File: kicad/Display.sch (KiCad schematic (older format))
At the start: 5 parts, among them SW301 SW_PUSH, U301 EA_DOGMxxx-A

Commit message: Change over to use the DOGM081 adapter board rather than direct connect - also used the CE_Socket!
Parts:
- removed C301: 0.1~~1μF, Capacitors_SMD:C_1206, symbol C
- removed C302: 0.47~~2.2μF, Capacitors_SMD:C_1206, symbol C
- removed U301: EA_DOGMxxx-A, FieldDevice_Footprints:EA_DOGM081x-A, symbol EA_DOGMxxx-A
- added P301: CONN_01X06, Pin_Headers:Pin_Header_Straight_1x06_Pitch2.54mm, symbol CONN_01X06
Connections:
- wire segments 37 -> 13
- no-connect marks 4 -> 0
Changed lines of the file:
@@
 Comment4 ""
 $EndDescr
-$Comp
-L EA_DOGMxxx-A U301
-U 1 1 593F5011
-P 5550 2850
-F 0 "U301" H 5400 3450 60  0000 C CNN
-F 1 "EA_DOGMxxx-A" H 5600 2850 60  0000 C CNN
-F 2 "FieldDevice_Footprints:EA_DOGM081x-A" V 4450 5200 60  0001 C CNN
-F 3 "" V 4450 5200 60  0000 C CNN
-F 4 "EA DOGM801W-A" H 5550 2850 60  0001 C CNN "MPN"
-F 5 "Value" H 5550 2850 60  0001 C CNN "Link"
-	1    5550 2850
-	1    0    0    -1
-$EndComp
-NoConn ~ 6350 1800
-NoConn ~ 6250 1800
-NoConn ~ 5150 1800
-NoConn ~ 5050 1800
-Wire Wire Line
-	6650 2700 7200 2700
-Text HLabel 7200 2700 2    60   Input ~ 0
+Text HLabel 5450 2650 0    60   Input ~ 0
+RS
+Text HLabel 5450 2350 0    60   Input ~ 0
 3V3
-Wire Wire Line
-	4450 2150 3850 2150
-$Comp
-L GND #PWR010
-U 1 1 593F50AA
-P 6900 2450
-F 0 "#PWR010" H 6900 2200 50  0001 C CNN
-F 1 "GND" H 6900 2300 50  0000 C CNN
-F 2 "" H 6900 2450 60  0000 C CNN
-F 3 "" H 6900 2450 60  0000 C CNN
-	1    6900 2450
-	1    0    0    -1
-$EndComp
-Wire Wire Line
-	6650 2400 6900 2400
-Wire Wire Line
-	6900 2400 6900 2450
-Wire Wire Line
-	5950 4100 5950 3900
-Wire Wire Line
-	5250 4100 5950 4100
-Wire Wire Line
-	5250 4100 5250 3900
-Wire Wire Line
-	5350 3900 5350 4100
-Connection ~ 5350 4100
-Wire Wire Line
-	5450 3900 5450 4100
-Connection ~ 5450 4100
-Wire Wire Line
-	5550 3900 5550 4100
-Connection ~ 5550 4100
-Wire Wire Line
-	5650 3900 5650 4100
-Connection ~ 5650 4100
-Wire Wire Line
-	5750 3900 5750 4100
-Connection ~ 5750 4100
-$Comp
-L GND #PWR011
-U 1 1 593F5140
-P 6050 4150
-F 0 "#PWR011" H 6050 3900 50  0001 C CNN
-F 1 "GND" H 6050 4000 50  0000 C CNN
-F 2 "" H 6050 4150 60  0000 C CNN
-F 3 "" H 6050 4150 60  0000 C CNN
-	1    6050 4150
-	1    0    0    -1
-$EndComp
-Wire Wire Line
-	6050 3900 6050 4150
-Wire Wire Line
-	6150 3900 6150 4500
-Wire Wire Line
-	6150 4500 5800 4500
-Text HLabel 5800 4500 0    60   Input ~ 0
-RS
-Text HLabel 5500 4300 0    60   Input ~ 0
-3V3
-$Comp
-L GND #PWR012
-U 1 1 593F51AC
-P 3250 2400
-F 0 "#PWR012" H 3250 2150 50  0001 C CNN
-F 1 "GND" H 3250 2250 50  0000 C CNN
-F 2 "" H 3250 2400 60  0000 C CNN
-F 3 "" H 3250 2400 60  0000 C CNN
-	1    3250 2400
-	1    0    0    -1
-$EndComp
-Wire Wire Line
-	3250 2400 3250 2350
-Wire Wire Line
-	3250 2350 4450 2350
-$Comp
-L C C301
-U 1 1 593F51D8
-P 4200 2750
-F 0 "C301" H 4225 2850 50  0000 L CNN
-F 1 "0.1~~1μF" H 4225 2650 50  0000 L CNN
-F 2 "Capacitors_SMD:C_1206" H 4238 2600 30  0001 C CNN
-F 3 "" H 4200 2750 60  0000 C CNN
-F 4 "X7R-G1206 1,0/50" H 4200 2750 60  0001 C CNN "MPN"
-F 5 "Value" H 4200 2750 60  0001 C CNN "Link"
-	1    4200 2750
-	-1   0    0    1
-$EndComp
-Wire Wire Line
-	4450 2600 4200 2600
-Wire Wire Line
-	4200 2900 4450 2900
-$Comp
-L C C302
-U 1 1 593F5875
-P 4200 3350
-F 0 "C302" H 4225 3450 50  0000 L CNN
-F 1 "0.47~~2.2μF" H 4225 3250 50  0000 L CNN
-F 2 "Capacitors_SMD:C_1206" H 4238 3200 30  0001 C CNN
-F 3 "" H 4200 3350 60  0000 C CNN
-F 4 "X7R-G1206 1,0/50" H 4200 3350 60  0001 C CNN "MPN"
-F 5 "Value" H 4200 3350 60  0001 C CNN "Link"
-	1    4200 3350
-	-1   0    0    1
-$EndComp
-Wire Wire Line
-	4200 3200 4450 3200
-Wire Wire Line
-	4200 3500 4450 3500
-Text HLabel 3900 3150 0    60   Input ~ 0
-3V3
-Wire Wire Line
-	3900 3150 4350 3150
-Wire Wire Line
-	4350 3150 4350 3200
-Connection ~ 4350 3200
-Wire Wire Line
-	5500 4300 5600 4300
-Wire Wire Line
-	5600 4300 5600 4100
-Connection ~ 5600 4100
-Wire Wire Line
-	5050 3900 5050 4100
-Wire Wire Line
-	5050 4100 4500 4100
-Wire Wire Line
-	5150 3900 5150 4200
-Wire Wire Line
-	5150 4200 4500 4200
-Text HLabel 4500 4100 0    60   Input ~ 0
+Text HLabel 5450 2450 0    60   Input ~ 0
 MOSI
-Text HLabel 4500 4200 0    60   Input ~ 0
+Text HLabel 5450 2550 0    60   Input ~ 0
 SCK
-Text HLabel 3850 2150 0    60   Input ~ 0
-3V3
-Wire Wire Line
-	6350 3900 6350 4650
-Wire Wire Line
-	6350 4650 5800 4650
-Text HLabel 5800 4650 0    60   Input ~ 0
+Text HLabel 5450 2750 0    60   Input ~ 0
 CS
 $Comp
@@
 $EndComp
 $Comp
-L GND #PWR013
+L GND #PWR010
 U 1 1 593FDBE4
 P 9450 2400
-F 0 "#PWR013" H 9450 2150 50  0001 C CNN
+F 0 "#PWR010" H 9450 2150 50  0001 C CNN
 F 1 "GND" H 9450 2250 50  0000 C CNN
 F 2 "" H 9450 2400 50  0000 C CNN
@@
 	1    0    0    -1
 $EndComp
-Wire Wire Line
-	9250 1500 9450 1500
-Wire Wire Line
-	9450 1500 9450 2400
-Wire Wire Line
-	8650 1500 8150 1500
 Text HLabel 8150 1500 0    60   Input ~ 0
 Display
@@
 $EndComp
 Wire Wire Line
+	9250 1500 9450 1500
+Wire Wire Line
+	9450 1500 9450 2400
+Wire Wire Line
+	8650 1500 8150 1500
+Wire Wire Line
 	8550 2200 8550 2300
 Wire Wire Line
@@
 	8550 1900 8550 1500
 Connection ~ 8550 1500
+$Comp
+L CONN_01X06 P301
+U 1 1 598B33D0
+P 5900 2600
+F 0 "P301" H 5900 2950 50  0000 C CNN
+F 1 "CONN_01X06" V 6000 2600 50  0000 C CNN
+F 2 "Pin_Headers:Pin_Header_Straight_1x06_Pitch2.54mm" H 5900 2600 60  0001 C CNN
+F 3 "" H 5900 2600 60  0000 C CNN
+	1    5900 2600
+	1    0    0    -1
+$EndComp
+Wire Wire Line
+	5700 2350 5450 2350
+Wire Wire Line
+	5700 2450 5450 2450
+Wire Wire Line
+	5700 2550 5450 2550
+Wire Wire Line
+	5700 2650 5450 2650
+Wire Wire Line
+	5700 2750 5450 2750
+Wire Wire Line
+	5700 2850 5400 2850
+Wire Wire Line
+	5400 2850 5400 3000
+$Comp
+L GND #PWR011
+U 1 1 598B3757
+P 5400 3000
+F 0 "#PWR011" H 5400 2750 50  0001 C CNN
+F 1 "GND" H 5400 2850 50  0000 C CNN
+F 2 "" H 5400 3000 60  0000 C CNN
+F 3 "" H 5400 3000 60  0000 C CNN
+	1    5400 3000
+	1    0    0    -1
+$EndComp
 $EndSCHEMATC

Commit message: Enhanced display port connector and layout - Submit to OSH Park
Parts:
- C303: footprint Capacitors_SMD:C_0805 -> Capacitors_SMD:C_0805_HandSoldering
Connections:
- net labels added: SPI_SCK
- net labels removed: SCK
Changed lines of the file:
@@
 MOSI
 Text HLabel 5450 2550 0    60   Input ~ 0
-SCK
+SPI_SCK
 Text HLabel 5450 2750 0    60   Input ~ 0
 CS
@@
 F 0 "C303" H 8575 2150 50  0000 L CNN
 F 1 "0.1μF" H 8575 1950 50  0000 L CNN
-F 2 "Capacitors_SMD:C_0805" H 8588 1900 30  0001 C CNN
+F 2 "Capacitors_SMD:C_0805_HandSoldering" H 8588 1900 30  0001 C CNN
 F 3 "" H 8550 2050 60  0000 C CNN
 	1    8550 2050

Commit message: Altered the display connector for the DOG104 i.e. general purpose
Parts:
- removed P301: CONN_01X06, Pin_Headers:Pin_Header_Straight_1x06_Pitch2.54mm, symbol CONN_01X06
- added P301: Conn_01x07_Female, Pin_Headers:Pin_Header_Angled_1x07_Pitch2.54mm, symbol Conn_01x07_Female
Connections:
- net labels added: MISO
- wire segments 13 -> 14
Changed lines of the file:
@@
 EESchema Schematic File Version 2
+LIBS:FieldDevice-rescue
 LIBS:fieldDevice_symbols
 LIBS:ce_header
@@
 Comment4 ""
 $EndDescr
-Text HLabel 5450 2650 0    60   Input ~ 0
+Text HLabel 5450 2750 0    60   Input ~ 0
 RS
 Text HLabel 5450 2350 0    60   Input ~ 0
@@
 Text HLabel 5450 2450 0    60   Input ~ 0
 MOSI
-Text HLabel 5450 2550 0    60   Input ~ 0
+Text HLabel 5450 2650 0    60   Input ~ 0
 SPI_SCK
-Text HLabel 5450 2750 0    60   Input ~ 0
+Text HLabel 5450 2850 0    60   Input ~ 0
 CS
 $Comp
@@
 $EndComp
 $Comp
-L GND #PWR010
+L GND #PWR09
 U 1 1 593FDBE4
 P 9450 2400
-F 0 "#PWR010" H 9450 2150 50  0001 C CNN
+F 0 "#PWR09" H 9450 2150 50  0001 C CNN
 F 1 "GND" H 9450 2250 50  0000 C CNN
 F 2 "" H 9450 2400 50  0000 C CNN
@@
 	8550 1900 8550 1500
 Connection ~ 8550 1500
-$Comp
-L CONN_01X06 P301
-U 1 1 598B33D0
-P 5900 2600
-F 0 "P301" H 5900 2950 50  0000 C CNN
-F 1 "CONN_01X06" V 6000 2600 50  0000 C CNN
-F 2 "Pin_Headers:Pin_Header_Straight_1x06_Pitch2.54mm" H 5900 2600 60  0001 C CNN
-F 3 "" H 5900 2600 60  0000 C CNN
-	1    5900 2600
-	1    0    0    -1
-$EndComp
 Wire Wire Line
 	5700 2350 5450 2350
@@
 	5700 2450 5450 2450
 Wire Wire Line
-	5700 2550 5450 2550
-Wire Wire Line
 	5700 2650 5450 2650
 Wire Wire Line
 	5700 2750 5450 2750
 Wire Wire Line
-	5700 2850 5400 2850
+	5700 2850 5450 2850
 Wire Wire Line
-	5400 2850 5400 3000
+	5700 2950 5400 2950
+Wire Wire Line
+	5400 2950 5400 3100
 $Comp
-L GND #PWR011
+L GND #PWR010
 U 1 1 598B3757
-P 5400 3000
-F 0 "#PWR011" H 5400 2750 50  0001 C CNN
-F 1 "GND" H 5400 2850 50  0000 C CNN
-F 2 "" H 5400 3000 60  0000 C CNN
-F 3 "" H 5400 3000 60  0000 C CNN
-	1    5400 3000
+P 5400 3100
+F 0 "#PWR010" H 5400 2850 50  0001 C CNN
+F 1 "GND" H 5400 2950 50  0000 C CNN
+F 2 "" H 5400 3100 60  0000 C CNN
+F 3 "" H 5400 3100 60  0000 C CNN
+	1    5400 3100
 	1    0    0    -1
 $EndComp
+$Comp
+L Conn_01x07_Female P301
+U 1 1 5A5666E2
+P 5900 2650
+F 0 "P301" H 5900 3050 50  0000 C CNN
+F 1 "Conn_01x07_Female" H 5900 2250 50  0000 C CNN
+F 2 "Pin_Headers:Pin_Header_Angled_1x07_Pitch2.54mm" H 5900 2650 50  0001 C CNN
+F 3 "" H 5900 2650 50  0001 C CNN
+	1    5900 2650
+	1    0    0    -1
+$EndComp
+Wire Wire Line
+	5700 2550 5450 2550
+Text HLabel 5450 2550 0    60   Input ~ 0
+MISO
 $EndSCHEMATC

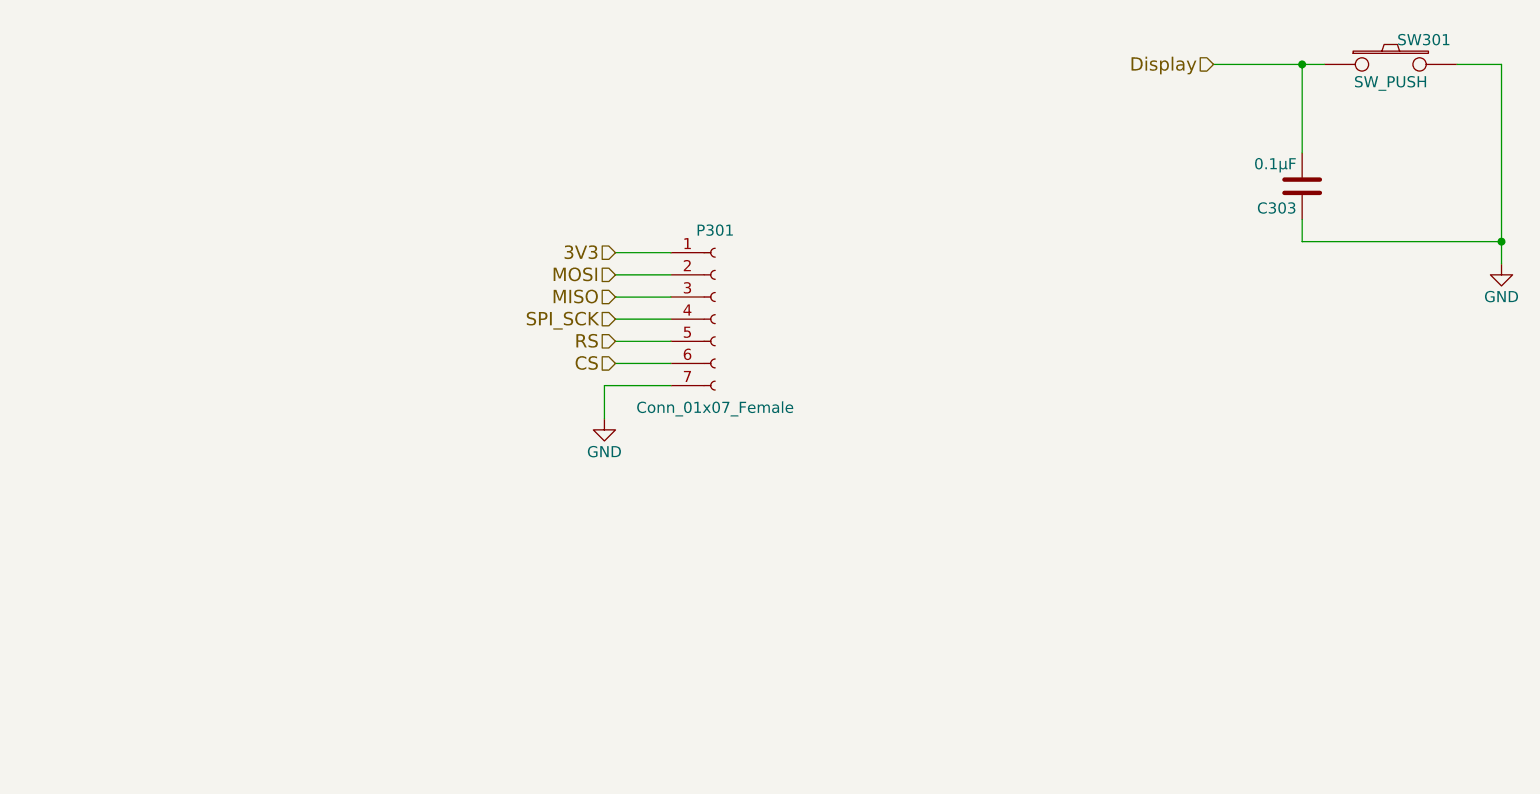
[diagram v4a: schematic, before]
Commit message: Revamping the schematic and layout for a deployable model
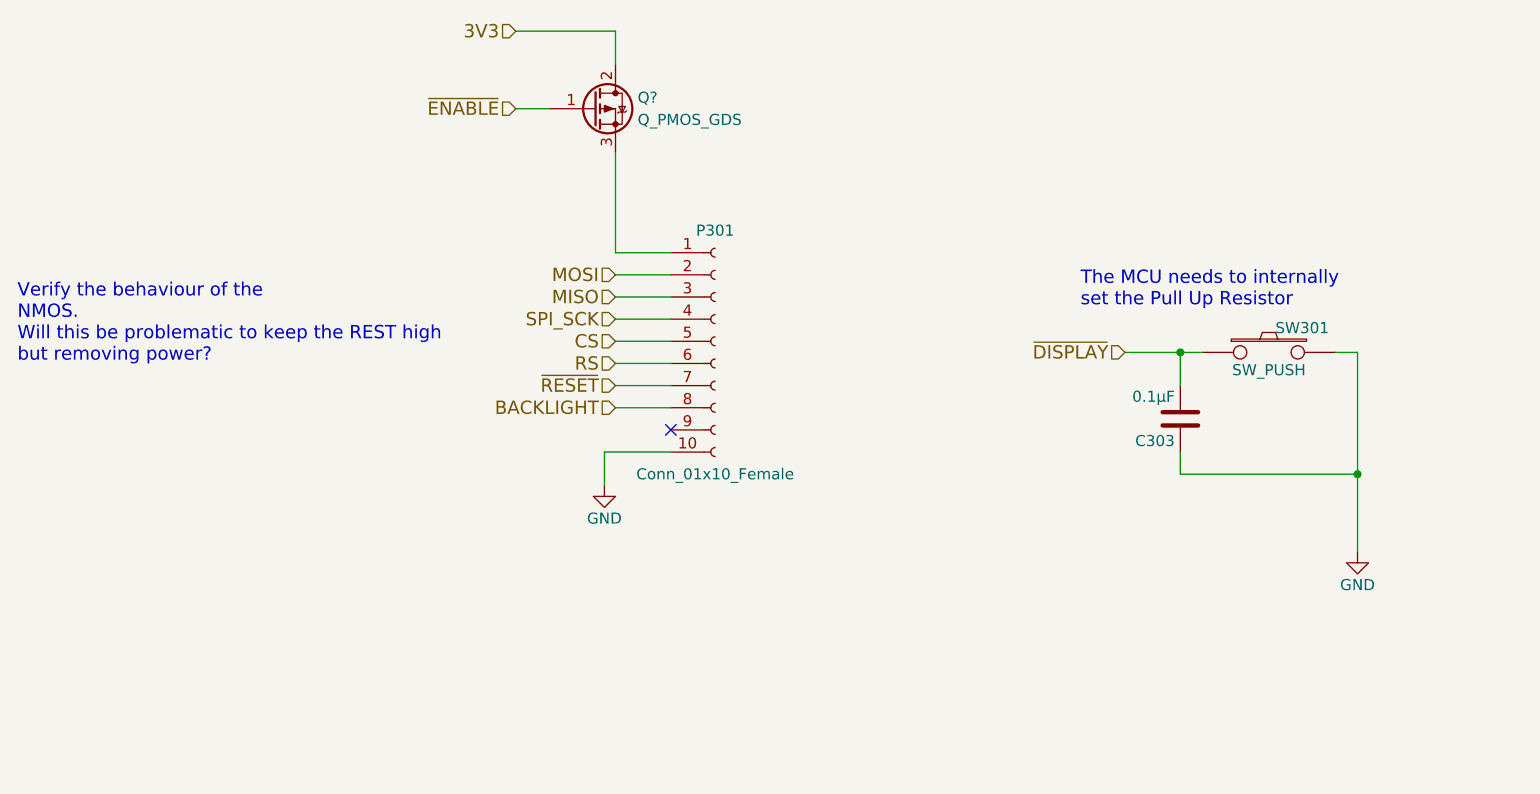
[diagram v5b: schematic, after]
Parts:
- removed P301: Conn_01x07_Female, Pin_Headers:Pin_Header_Angled_1x07_Pitch2.54mm, symbol Conn_01x07_Female
- added P301: Conn_01x10_Female, symbol Conn_01x10_Female
- added Q?: Q_PMOS_GDS, symbol Q_PMOS_GDS
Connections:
- net 3V3: now also Q?.2 (D)
- net CS: now also P301.5 (Pin_5)
- net GND: now also P301.10 (Pin_10)
- net MISO: now also P301.3 (Pin_3)
- net MOSI: now also P301.2 (Pin_2)
- net RS: now also P301.6 (Pin_6)
- net SPI_SCK: now also P301.4 (Pin_4)
- net Display renamed ~DISPLAY
- new net: P301.1 (Pin_1), Q?.3 (S)
- new net BACKLIGHT: P301.8 (Pin_8)
- new net ~ENABLE: Q?.1 (G)
- new net ~RESET: P301.7 (Pin_7)
- no-connect marks 0 -> 1
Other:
- note added: "The MCU needs to internally \nset the Pull Up Resistor"
- note added: "Verify the behaviour of the \nNMOS.\nWill this be problematic to keep the REST high\nbut removing power?"
- moved on the sheet: C303, SW301
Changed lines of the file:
@@
 Comment4 ""
 $EndDescr
-Text HLabel 5450 2750 0    60   Input ~ 0
+Text HLabel 5450 2850 0    60   Input ~ 0
 RS
-Text HLabel 5450 2350 0    60   Input ~ 0
+Text HLabel 5000 1350 0    60   Input ~ 0
 3V3
 Text HLabel 5450 2450 0    60   Input ~ 0
@@
 Text HLabel 5450 2650 0    60   Input ~ 0
 SPI_SCK
-Text HLabel 5450 2850 0    60   Input ~ 0
+Text HLabel 5450 2750 0    60   Input ~ 0
 CS
 $Comp
 L SW_PUSH SW301
 U 1 1 593FDBDD
-P 8950 1500
-F 0 "SW301" H 9100 1610 50  0000 C CNN
-F 1 "SW_PUSH" H 8950 1420 50  0000 C CNN
-F 2 "Pin_Headers:Pin_Header_Straight_1x02_Pitch2.54mm" H 8950 1500 60  0001 C CNN
-F 3 "" H 8950 1500 60  0000 C CNN
-	1    8950 1500
+P 8400 2800
+F 0 "SW301" H 8550 2910 50  0000 C CNN
+F 1 "SW_PUSH" H 8400 2720 50  0000 C CNN
+F 2 "Pin_Headers:Pin_Header_Straight_1x02_Pitch2.54mm" H 8400 2800 60  0001 C CNN
+F 3 "" H 8400 2800 60  0000 C CNN
+	1    8400 2800
 	1    0    0    -1
 $EndComp
@@
 L GND #PWR09
 U 1 1 593FDBE4
-P 9450 2400
-F 0 "#PWR09" H 9450 2150 50  0001 C CNN
-F 1 "GND" H 9450 2250 50  0000 C CNN
-F 2 "" H 9450 2400 50  0000 C CNN
-F 3 "" H 9450 2400 50  0000 C CNN
-	1    9450 2400
+P 8800 3700
+F 0 "#PWR09" H 8800 3450 50  0001 C CNN
+F 1 "GND" H 8800 3550 50  0000 C CNN
+F 2 "" H 8800 3700 50  0000 C CNN
+F 3 "" H 8800 3700 50  0000 C CNN
+	1    8800 3700
 	1    0    0    -1
 $EndComp
-Text HLabel 8150 1500 0    60   Input ~ 0
-Display
+Text HLabel 7750 2800 0    60   Input ~ 0
+~DISPLAY
 $Comp
 L C C303
 U 1 1 59402950
-P 8550 2050
-F 0 "C303" H 8575 2150 50  0000 L CNN
-F 1 "0.1μF" H 8575 1950 50  0000 L CNN
-F 2 "Capacitors_SMD:C_0805_HandSoldering" H 8588 1900 30  0001 C CNN
-F 3 "" H 8550 2050 60  0000 C CNN
-	1    8550 2050
+P 8000 3100
+F 0 "C303" H 8025 3200 50  0000 L CNN
+F 1 "0.1μF" H 8025 3000 50  0000 L CNN
+F 2 "Capacitors_SMD:C_0805_HandSoldering" H 8038 2950 30  0001 C CNN
+F 3 "" H 8000 3100 60  0000 C CNN
+	1    8000 3100
 	-1   0    0    1
 $EndComp
 Wire Wire Line
-	9250 1500 9450 1500
+	8700 2800 8800 2800
 Wire Wire Line
-	9450 1500 9450 2400
+	8800 2800 8800 3350
 Wire Wire Line
-	8650 1500 8150 1500
+	8800 3350 8800 3700
 Wire Wire Line
-	8550 2200 8550 2300
+	7750 2800 8000 2800
 Wire Wire Line
-	8550 2300 9450 2300
-Connection ~ 9450 2300
+	8000 2800 8100 2800
 Wire Wire Line
-	8550 1900 8550 1500
-Connection ~ 8550 1500
+	8000 3250 8000 3350
+Wire Wire Line
+	8000 3350 8800 3350
+Connection ~ 8800 3350
+Wire Wire Line
+	8000 2950 8000 2800
+Connection ~ 8000 2800
 Wire Wire Line
 	5700 2350 5450 2350
@@
 	5700 2850 5450 2850
 Wire Wire Line
-	5700 2950 5400 2950
+	5700 2950 5450 2950
 Wire Wire Line
-	5400 2950 5400 3100
+	5400 3250 5400 3400
 $Comp
 L GND #PWR010
 U 1 1 598B3757
-P 5400 3100
-F 0 "#PWR010" H 5400 2850 50  0001 C CNN
-F 1 "GND" H 5400 2950 50  0000 C CNN
-F 2 "" H 5400 3100 60  0000 C CNN
-F 3 "" H 5400 3100 60  0000 C CNN
-	1    5400 3100
-	1    0    0    -1
-$EndComp
-$Comp
-L Conn_01x07_Female P301
-U 1 1 5A5666E2
-P 5900 2650
-F 0 "P301" H 5900 3050 50  0000 C CNN
-F 1 "Conn_01x07_Female" H 5900 2250 50  0000 C CNN
-F 2 "Pin_Headers:Pin_Header_Angled_1x07_Pitch2.54mm" H 5900 2650 50  0001 C CNN
-F 3 "" H 5900 2650 50  0001 C CNN
-	1    5900 2650
+P 5400 3400
+F 0 "#PWR010" H 5400 3150 50  0001 C CNN
+F 1 "GND" H 5400 3250 50  0000 C CNN
+F 2 "" H 5400 3400 60  0000 C CNN
+F 3 "" H 5400 3400 60  0000 C CNN
+	1    5400 3400
 	1    0    0    -1
 $EndComp
@@
 Text HLabel 5450 2550 0    60   Input ~ 0
 MISO
+$Comp
+L Conn_01x10_Female P301
+U 1 1 5A6CD6E7
+P 5900 2750
+F 0 "P301" H 5900 3250 50  0000 C CNN
+F 1 "Conn_01x10_Female" H 5900 2150 50  0000 C CNN
+F 2 "" H 5900 2750 50  0001 C CNN
+F 3 "" H 5900 2750 50  0001 C CNN
+	1    5900 2750
+	1    0    0    -1
+$EndComp
+Wire Wire Line
+	5700 3250 5400 3250
+Text HLabel 5450 2950 0    60   Input ~ 0
+~RESET
+Wire Wire Line
+	5700 3050 5450 3050
+Text HLabel 5450 3050 0    60   Input ~ 0
+BACKLIGHT
+NoConn ~ 5700 3150
+Wire Wire Line
+	5150 1700 5000 1700
+Wire Wire Line
+	5450 1500 5450 1350
+Wire Wire Line
+	5450 1350 5000 1350
+Text HLabel 5000 1700 0    60   Input ~ 0
+~ENABLE
+Wire Wire Line
+	5450 2350 5450 1900
+Text Notes 7550 2600 0    60   ~ 0
+The MCU needs to internally \nset the Pull Up Resistor
+$Comp
+L Q_PMOS_GDS Q?
+U 1 1 5A6D0129
+P 5350 1700
+F 0 "Q?" H 5550 1750 50  0000 L CNN
+F 1 "Q_PMOS_GDS" H 5550 1650 50  0000 L CNN
+F 2 "" H 5550 1800 50  0001 C CNN
+F 3 "" H 5350 1700 50  0001 C CNN
+	1    5350 1700
+	1    0    0    -1
+$EndComp
+Text Notes 2750 2850 0    60   ~ 0
+Verify the behaviour of the \nNMOS.\nWill this be problematic to keep the REST high\nbut removing power?
 $EndSCHEMATC
